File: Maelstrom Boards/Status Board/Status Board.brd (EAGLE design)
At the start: 101.6 x 76.2 mm, 28 parts, among them IC1 LM555D, P1 39-30-04?, Q1 310mA/60V/1.6Ω

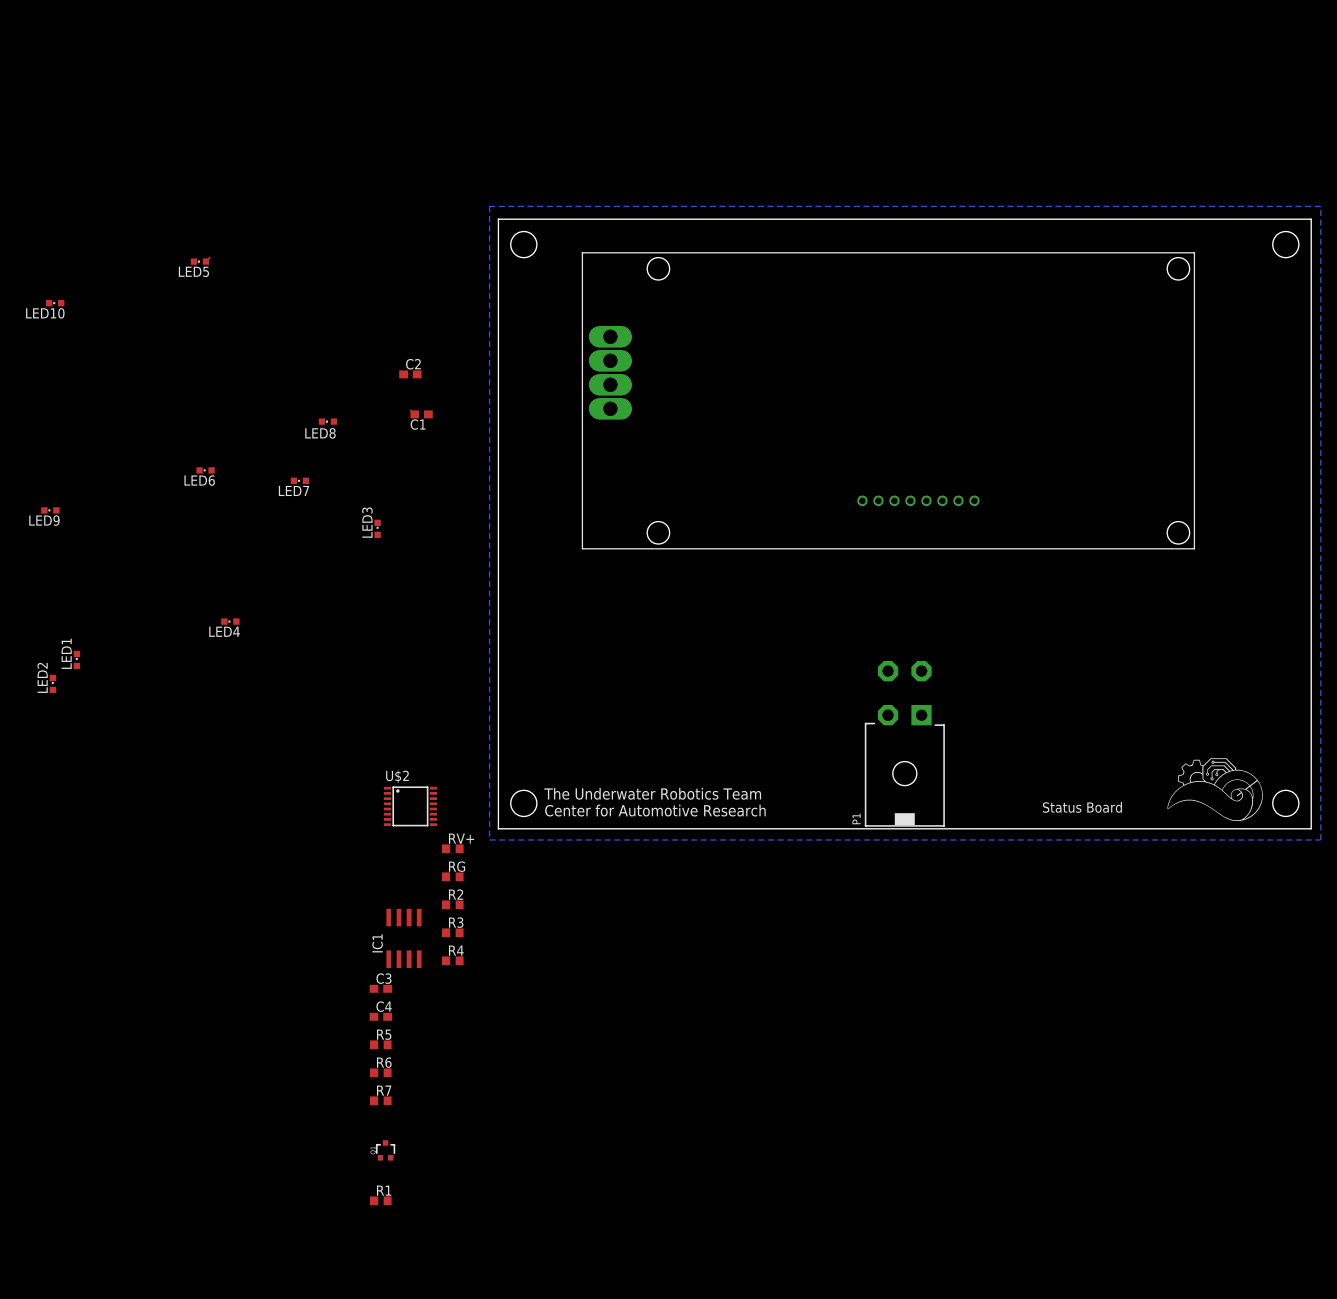
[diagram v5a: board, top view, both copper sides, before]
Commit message: Adding caps and fixing screen
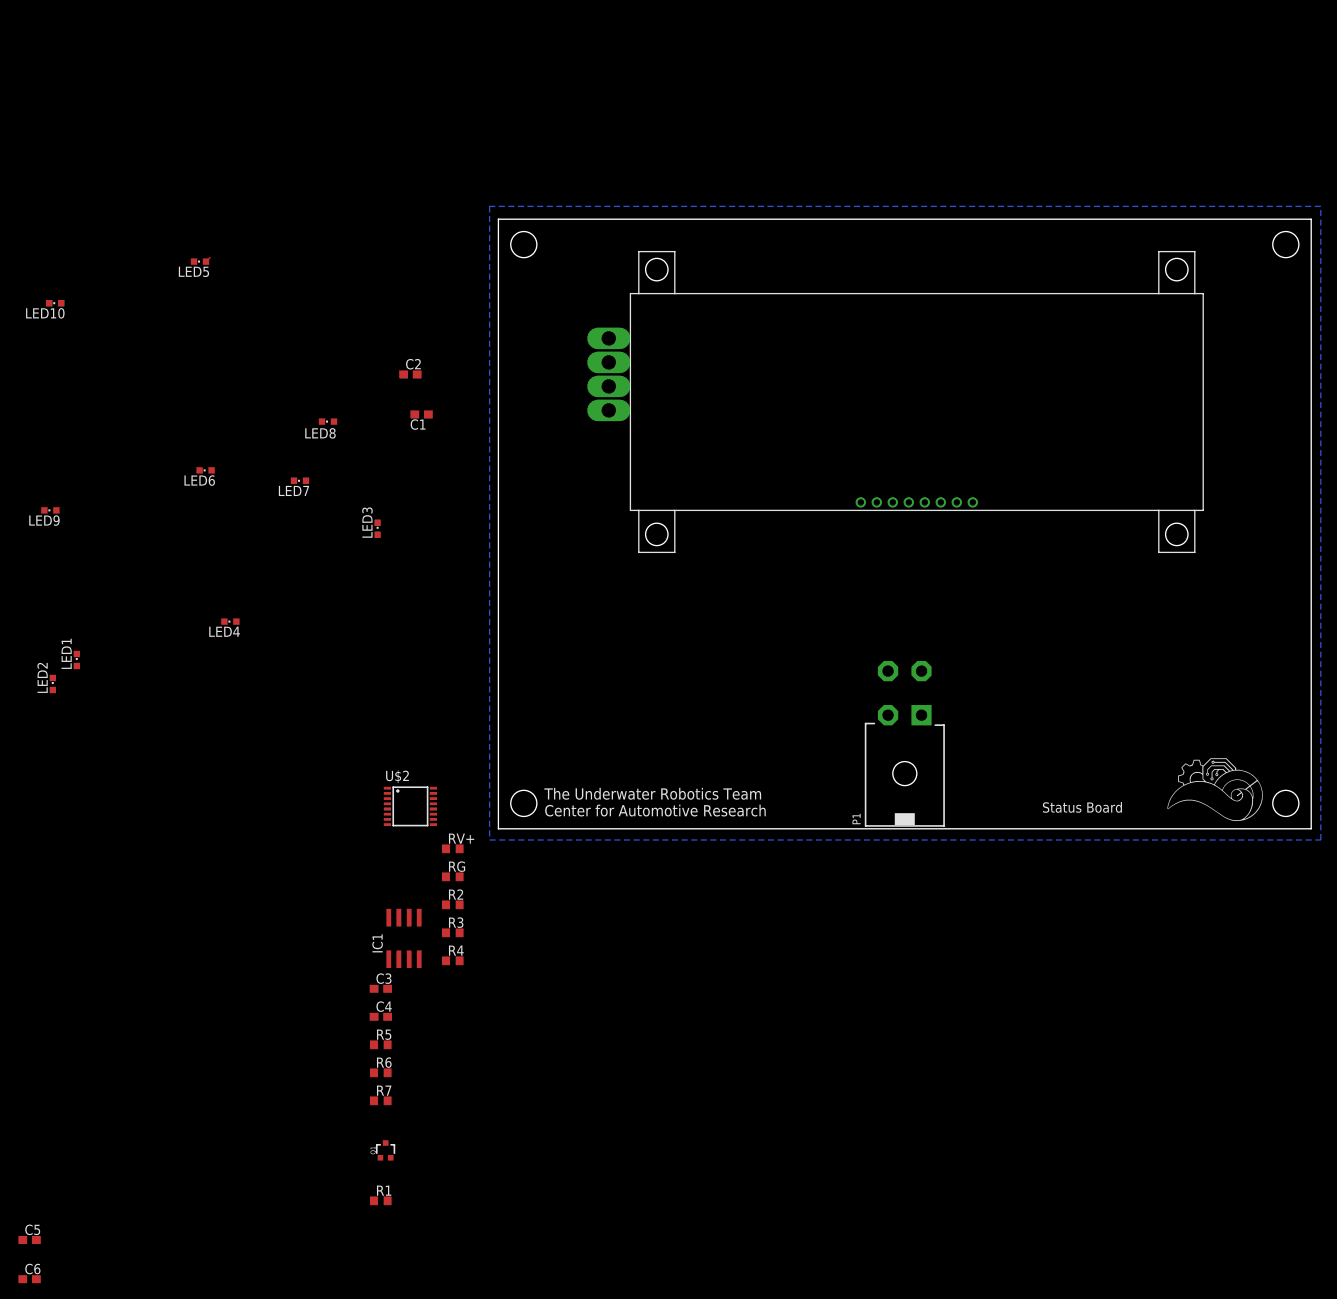
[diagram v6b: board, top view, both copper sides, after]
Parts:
- added C5: 0.047uF, rcl:C0603
- added C6: 0.01uF, rcl:C0603
- moved U$1 0.28 mm to (19.8, 36.8)
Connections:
- new net N$8: C6.2, IC1.5
- net +3V3: now also C5.1
- net GND: now also C1.1, C5.2, C6.1; no longer C1.2
- net N$3: now also C1.2; no longer C1.1
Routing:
- net GND: track 0.78 -> 0.00 mm
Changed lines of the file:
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@@
 </autorouter>
 <elements>
-<element name="U$1" library="NHD-C0220BiZ" package="NHD-C0220BIZ" value="NHD-C0220BIZ" x="20" y="37" smashed="yes"/>
+<element name="U$1" library="NHD-C0220BiZ" package="NHD-C0220BIZ" value="NHD-C0220BIZ" x="19.8" y="36.8" smashed="yes"/>
 <element name="P1" library="con-molex-mini-fit" package="39-30-?04?" value="39-30-04?" x="50.8" y="14.2" smashed="yes">
 <attribute name="NAME" x="45.2755" y="0.4459" size="1.016" layer="25" ratio="18" rot="R90"/>
@@
 <attribute name="SPICEPREFIX" value="R" x="-14.7" y="-46.5" size="1.778" layer="27" display="off"/>
 <attribute name="VALUE" x="-15.335" y="-48.405" size="1.27" layer="27"/>
+</element>
+<element name="C5" library="rcl" library_urn="urn:adsk.eagle:library:334" package="C0603" package3d_urn="urn:adsk.eagle:package:23616/2" value="0.047uF" x="-58.6" y="-51.4" smashed="yes">
+<attribute name="NAME" x="-59.235" y="-50.765" size="1.27" layer="25"/>
+<attribute name="SPICEPREFIX" value="C" x="-58.6" y="-51.4" size="1.778" layer="27" display="off"/>
+<attribute name="VALUE" x="-59.235" y="-53.305" size="1.27" layer="27"/>
+</element>
+<element name="C6" library="rcl" library_urn="urn:adsk.eagle:library:334" package="C0603" package3d_urn="urn:adsk.eagle:package:23616/2" value="0.01uF" x="-58.6" y="-56.3" smashed="yes">
+<attribute name="NAME" x="-59.235" y="-55.665" size="1.27" layer="25"/>
+<attribute name="SPICEPREFIX" value="C" x="-58.6" y="-56.3" size="1.778" layer="27" display="off"/>
+<attribute name="VALUE" x="-59.235" y="-58.205" size="1.27" layer="27"/>
 </element>
 </elements>
@@
 <contactref element="U$2" pad="8"/>
 <contactref element="RG" pad="1"/>
-<contactref element="IC1" pad="1"/>
 <contactref element="C4" pad="2"/>
 <contactref element="C3" pad="2"/>
 <contactref element="Q1" pad="2"/>
-<contactref element="U$1" pad="VSS"/>
-<contactref element="C1" pad="2"/>
-<wire x1="-10.45" y1="51.8" x2="-11" y2="52.35" width="0.1524" layer="1"/>
 <polygon width="0.1524" layer="16">
 <vertex x="-1.1" y="77.8"/>
@@
 <vertex x="102.8" y="77.8"/>
 </polygon>
+<contactref element="C5" pad="2"/>
+<contactref element="C6" pad="1"/>
+<contactref element="IC1" pad="1"/>
+<contactref element="U$1" pad="VSS"/>
+<contactref element="C1" pad="1"/>
+<wire x1="-57.75" y1="-51.4" x2="-59.45" y2="-56.3" width="0" layer="19" extent="1-1"/>
+<wire x1="-13.45" y1="-41.125" x2="-57.75" y2="-51.4" width="0" layer="19" extent="1-1"/>
 <wire x1="-13.85" y1="-23.5" x2="-13.45" y2="-41.125" width="0" layer="19" extent="1-1"/>
 <wire x1="-13.85" y1="-20" x2="-13.85" y2="-23.5" width="0" layer="19" extent="1-1"/>
@@
 <wire x1="-6.55" y1="-6" x2="-13.705" y2="-16.3" width="0" layer="19" extent="1-1"/>
 <wire x1="-13.875" y1="0.525" x2="-6.55" y2="-6" width="0" layer="19" extent="1-1"/>
-<wire x1="-10.45" y1="51.8" x2="-13.875" y2="0.525" width="0" layer="19" extent="1-1"/>
+<wire x1="-8.75" y1="51.8" x2="-13.875" y2="0.525" width="0" layer="19" extent="1-1"/>
 <wire x1="48.7045" y1="19.7118" x2="-6.55" y2="-6" width="0" layer="19" extent="1-1"/>
+<wire x1="51.3" y1="40.8" x2="48.7045" y2="19.7118" width="0" layer="19" extent="1-1"/>
 </signal>
 <signal name="+3V3">
@@
 <contactref element="R7" pad="1"/>
 <contactref element="R1" pad="2"/>
-<wire x1="45.5" y1="41" x2="53.5" y2="41" width="0" layer="19" extent="1-1"/>
-<wire x1="48.7045" y1="14.2" x2="45.5" y2="41" width="0" layer="19" extent="1-1"/>
-<wire x1="14" y1="61.5" x2="45.5" y2="41" width="0" layer="19" extent="1-1"/>
-<wire x1="-4.85" y1="-2.5" x2="48.7045" y2="14.2" width="0" layer="19" extent="1-1"/>
+<contactref element="C5" pad="1"/>
+<wire x1="-13.85" y1="-46.5" x2="-59.45" y2="-51.4" width="0" layer="19" extent="1-1"/>
+<wire x1="-15.55" y1="-34" x2="-13.85" y2="-46.5" width="0" layer="19" extent="1-1"/>
+<wire x1="-13.85" y1="-30.5" x2="-15.55" y2="-34" width="0" layer="19" extent="1-1"/>
+<wire x1="-15.55" y1="-23.5" x2="-13.85" y2="-30.5" width="0" layer="19" extent="1-1"/>
+<wire x1="-13.705" y1="-11.1" x2="-15.55" y2="-23.5" width="0" layer="19" extent="1-1"/>
+<wire x1="-4.85" y1="-2.5" x2="-13.705" y2="-11.1" width="0" layer="19" extent="1-1"/>
 <wire x1="-8.125" y1="5.075" x2="-4.85" y2="-2.5" width="0" layer="19" extent="1-1"/>
-<wire x1="-13.705" y1="-11.1" x2="-4.85" y2="-2.5" width="0" layer="19" extent="1-1"/>
-<wire x1="-15.55" y1="-23.5" x2="-13.705" y2="-11.1" width="0" layer="19" extent="1-1"/>
-<wire x1="-13.85" y1="-30.5" x2="-15.55" y2="-23.5" width="0" layer="19" extent="1-1"/>
-<wire x1="-15.55" y1="-34" x2="-13.85" y2="-30.5" width="0" layer="19" extent="1-1"/>
-<wire x1="-13.85" y1="-46.5" x2="-15.55" y2="-34" width="0" layer="19" extent="1-1"/>
+<wire x1="48.7045" y1="14.2" x2="-4.85" y2="-2.5" width="0" layer="19" extent="1-1"/>
+<wire x1="45.3" y1="40.8" x2="48.7045" y2="14.2" width="0" layer="19" extent="1-1"/>
+<wire x1="53.3" y1="40.8" x2="45.3" y2="40.8" width="0" layer="19" extent="1-1"/>
+<wire x1="13.8" y1="61.3" x2="45.3" y2="40.8" width="0" layer="19" extent="1-1"/>
 </signal>
 <signal name="SDA">
@@
 <contactref element="U$1" pad="SDA"/>
 <contactref element="U$2" pad="15"/>
-<wire x1="52.8955" y1="14.2" x2="49.5" y2="41" width="0" layer="19" extent="1-1"/>
+<wire x1="52.8955" y1="14.2" x2="49.3" y2="40.8" width="0" layer="19" extent="1-1"/>
 <wire x1="-8.125" y1="4.425" x2="52.8955" y2="14.2" width="0" layer="19" extent="1-1"/>
 </signal>
@@
 <wire x1="52.7955" y1="19.8118" x2="52.8955" y2="19.7118" width="0.1524" layer="1"/>
 <contactref element="U$2" pad="14"/>
-<wire x1="52.7955" y1="19.8118" x2="47.5" y2="41" width="0" layer="19" extent="1-1"/>
+<wire x1="52.7955" y1="19.8118" x2="47.3" y2="40.8" width="0" layer="19" extent="1-1"/>
 <wire x1="-8.125" y1="3.775" x2="52.7955" y2="19.8118" width="0" layer="19" extent="1-1"/>
-</signal>
-<signal name="N$3">
-<contactref element="U$1" pad="VOUT"/>
-<contactref element="C1" pad="1"/>
-<wire x1="-8.75" y1="51.8" x2="55.5" y2="41" width="0" layer="19" extent="1-1"/>
 </signal>
 <signal name="RED">
@@
 <wire x1="-56.15" y1="65.7" x2="-38.05" y2="70.9" width="0" layer="19" extent="1-1"/>
 </signal>
+<signal name="N$7">
+<contactref element="R2" pad="1"/>
+<contactref element="U$1" pad="RK"/>
+<wire x1="-6.55" y1="-9.5" x2="13.8" y2="58.3" width="0" layer="19" extent="1-1"/>
+</signal>
+<signal name="N$8">
+<contactref element="IC1" pad="5"/>
+<contactref element="C6" pad="2"/>
+<wire x1="-9.895" y1="-11.1" x2="-57.75" y2="-56.3" width="0" layer="19" extent="1-1"/>
+</signal>
+<signal name="N$1">
+<contactref element="R3" pad="1"/>
+<contactref element="U$1" pad="GK"/>
+<wire x1="-6.55" y1="-13" x2="13.8" y2="55.3" width="0" layer="19" extent="1-1"/>
+</signal>
+<signal name="N$5">
+<contactref element="R4" pad="1"/>
+<contactref element="U$1" pad="BK"/>
+<wire x1="-6.55" y1="-16.5" x2="13.8" y2="52.3" width="0" layer="19" extent="1-1"/>
+</signal>
 <signal name="N$2">
 <contactref element="U$1" pad="C1-"/>
 <contactref element="C2" pad="1"/>
-<wire x1="-11.85" y1="56.8" x2="59.5" y2="41" width="0" layer="19" extent="1-1"/>
+<wire x1="-11.85" y1="56.8" x2="59.3" y2="40.8" width="0" layer="19" extent="1-1"/>
 </signal>
 <signal name="N$4">
+<contactref element="U$1" pad="C1+"/>
 <contactref element="C2" pad="2"/>
-<contactref element="U$1" pad="C1+"/>
-<wire x1="-10.15" y1="56.8" x2="57.5" y2="41" width="0" layer="19" extent="1-1"/>
-</signal>
-<signal name="N$1">
-<contactref element="R4" pad="1"/>
-<contactref element="U$1" pad="BK"/>
-<wire x1="-6.55" y1="-16.5" x2="14" y2="52.5" width="0" layer="19" extent="1-1"/>
-</signal>
-<signal name="N$5">
-<contactref element="U$1" pad="GK"/>
-<contactref element="R3" pad="1"/>
-<wire x1="-6.55" y1="-13" x2="14" y2="55.5" width="0" layer="19" extent="1-1"/>
-</signal>
-<signal name="N$7">
-<contactref element="R2" pad="1"/>
-<contactref element="U$1" pad="RK"/>
-<wire x1="-6.55" y1="-9.5" x2="14" y2="58.5" width="0" layer="19" extent="1-1"/>
+<wire x1="-10.15" y1="56.8" x2="57.3" y2="40.8" width="0" layer="19" extent="1-1"/>
+</signal>
+<signal name="N$3">
+<contactref element="C1" pad="2"/>
+<contactref element="U$1" pad="VOUT"/>
+<wire x1="-10.45" y1="51.8" x2="55.3" y2="40.8" width="0" layer="19" extent="1-1"/>
 </signal>
 </signals>

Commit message: Status Board Layout wiring connections
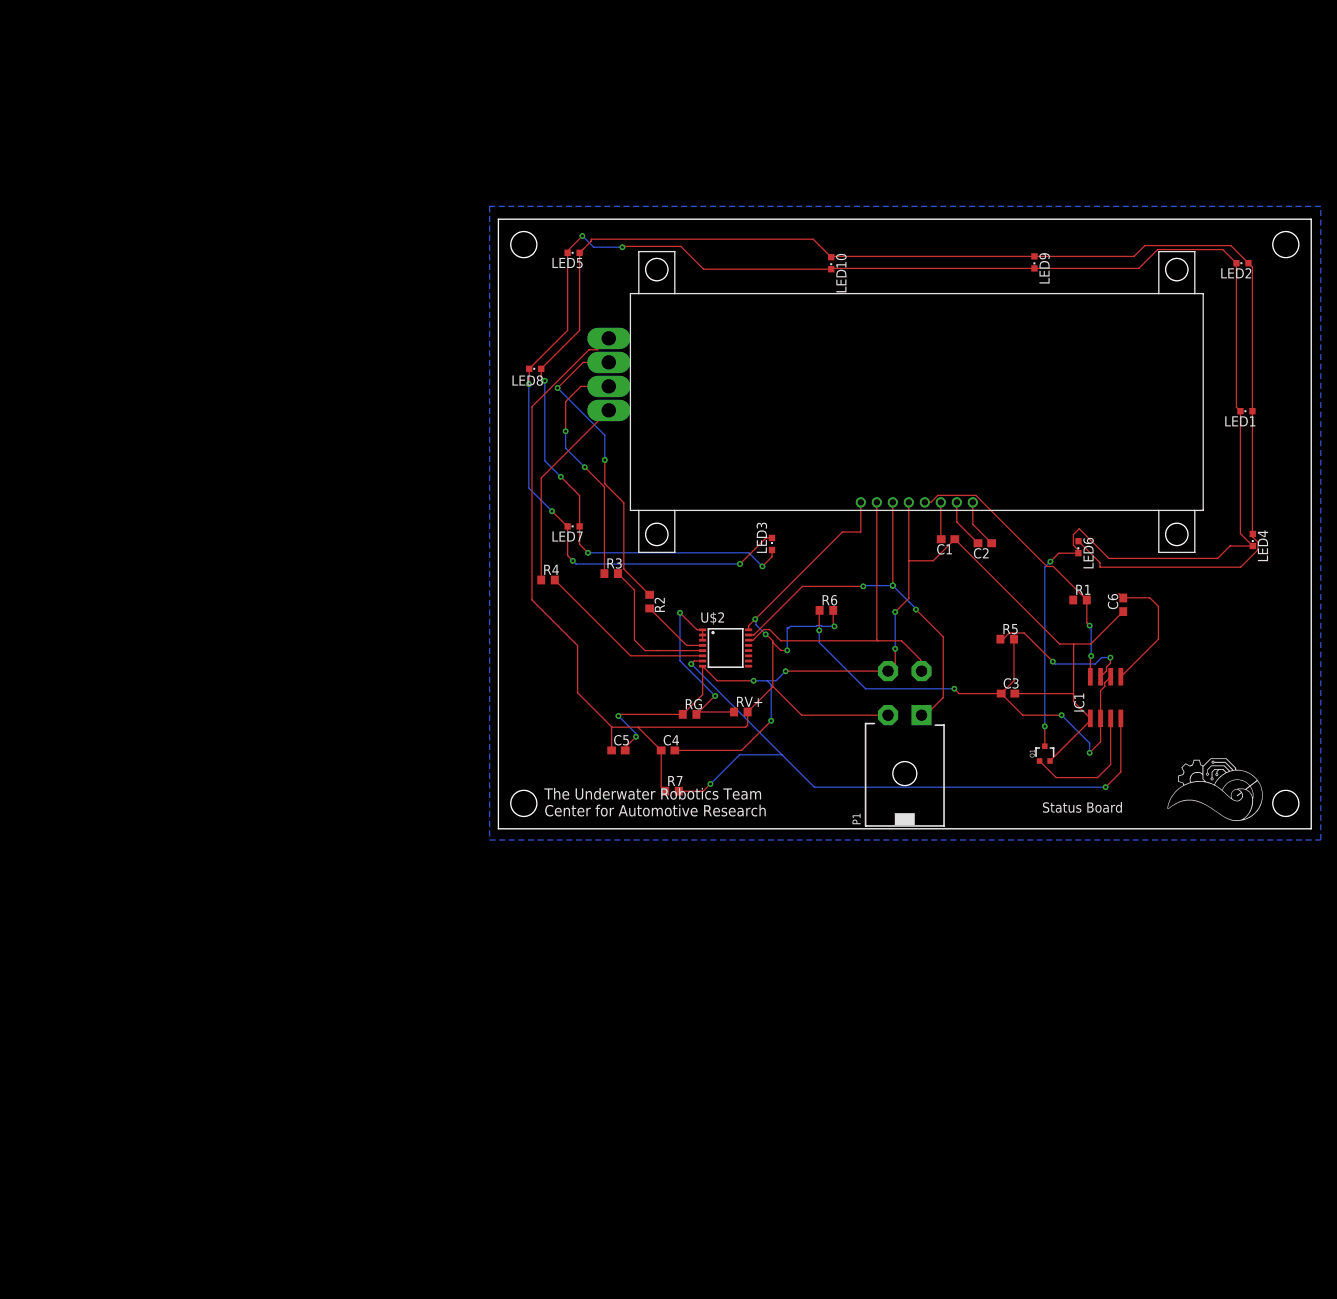
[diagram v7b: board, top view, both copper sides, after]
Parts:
- moved C6 160.6 mm to (78.1, 28.0), turned to 90 degrees
- moved LED2 157.7 mm to (93.0, 70.7), turned to 90 degrees
- moved LED1 149.5 mm to (93.5, 52.2), turned to 90 degrees
- moved LED4 128.2 mm to (94.3, 36.1), turned to 180 degrees
- moved LED9 126.8 mm to (67.0, 70.8), turned to 180 degrees
- moved R1 115.2 mm to (72.7, 28.6)
- moved LED6 109.5 mm to (72.5, 35.2), turned to 180 degrees
- moved LED10 97.1 mm to (41.6, 70.7), turned to 180 degrees
- moved Q1 96.2 mm to (68.3, 9.40)
- moved C5 95.7 mm to (15.0, 9.80)
- moved R5 93.3 mm to (63.6, 23.7)
- moved IC1 92.7 mm to (75.9, 16.4)
- moved C3 86.6 mm to (63.7, 16.9)
- moved R6 80.3 mm to (41.0, 27.3)
- moved C2 74.8 mm to (60.8, 35.7), turned to 180 degrees
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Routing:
- net N$20: track 0.53 -> 248.4 mm, vias 0 -> 8
- net N$11: track 0.71 -> 215.9 mm, vias 0 -> 4
- net +3V3: track 0.00 -> 190.3 mm, vias 0 -> 6
- net GND: track 0.00 -> 146.4 mm, vias 0 -> 7
- net BLINK_OFF: track 0.00 -> 83.9 mm, vias 0 -> 3
- net N$10: track 0.00 -> 62.3 mm, vias 0 -> 4
- net SDA: track 0.00 -> 51.5 mm, vias 0 -> 4
- net SCL: track 0.14 -> 42.4 mm
- net N$7: track 0.00 -> 38.3 mm, vias 0 -> 2
- net N$1: track 0.00 -> 29.7 mm, vias 0 -> 2
- net N$6: track 0.00 -> 25.4 mm, vias 0 -> 2
- net N$5: track 0.00 -> 24.7 mm
- net BLUE: track 0.00 -> 22.4 mm
- net N$9: track 0.00 -> 18.9 mm, vias 0 -> 2
- net GREEN: track 0.00 -> 18.3 mm
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
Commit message: Update Status Board
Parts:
- moved C6 9.84 mm to (82.3, 19.1)
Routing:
- net GND: track 146.4 -> 25.7 mm, vias 7 -> 10
- net N$11: track 215.9 -> 229.1 mm, vias 4 -> 6
- net +3V3: track 190.3 -> 202.0 mm
- net N$8: track 16.4 -> 4.91 mm
- net N$20: track 248.4 -> 252.9 mm
- net N$6: track 25.4 -> 24.0 mm
- net BLINK_OFF: track 83.9 -> 83.1 mm
- net N$9: track 18.9 -> 19.7 mm
- net SDA: track 51.5 -> 51.2 mm, vias 4 -> 2
- net N$10: track 62.3 -> 62.5 mm, vias 4 -> 6
